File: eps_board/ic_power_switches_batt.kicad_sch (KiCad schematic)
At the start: 4 parts, among them U47 MCP23008T-E/SS

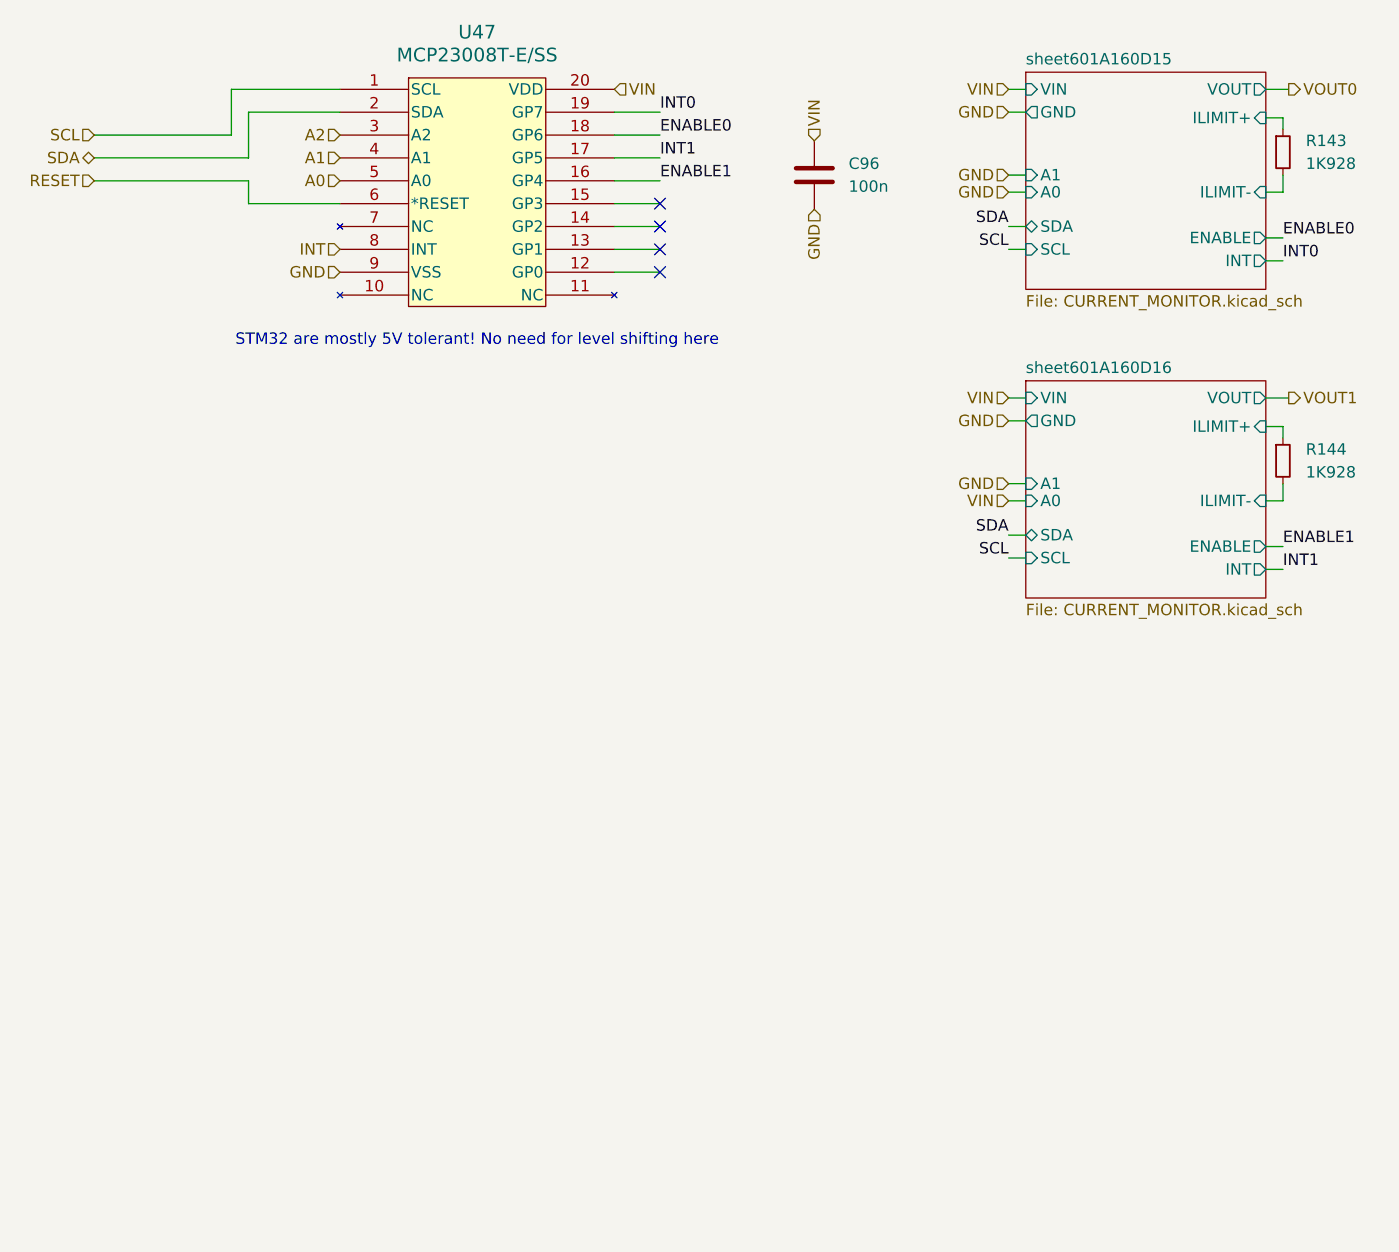
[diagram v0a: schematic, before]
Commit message: simply eps and automate startup conditions
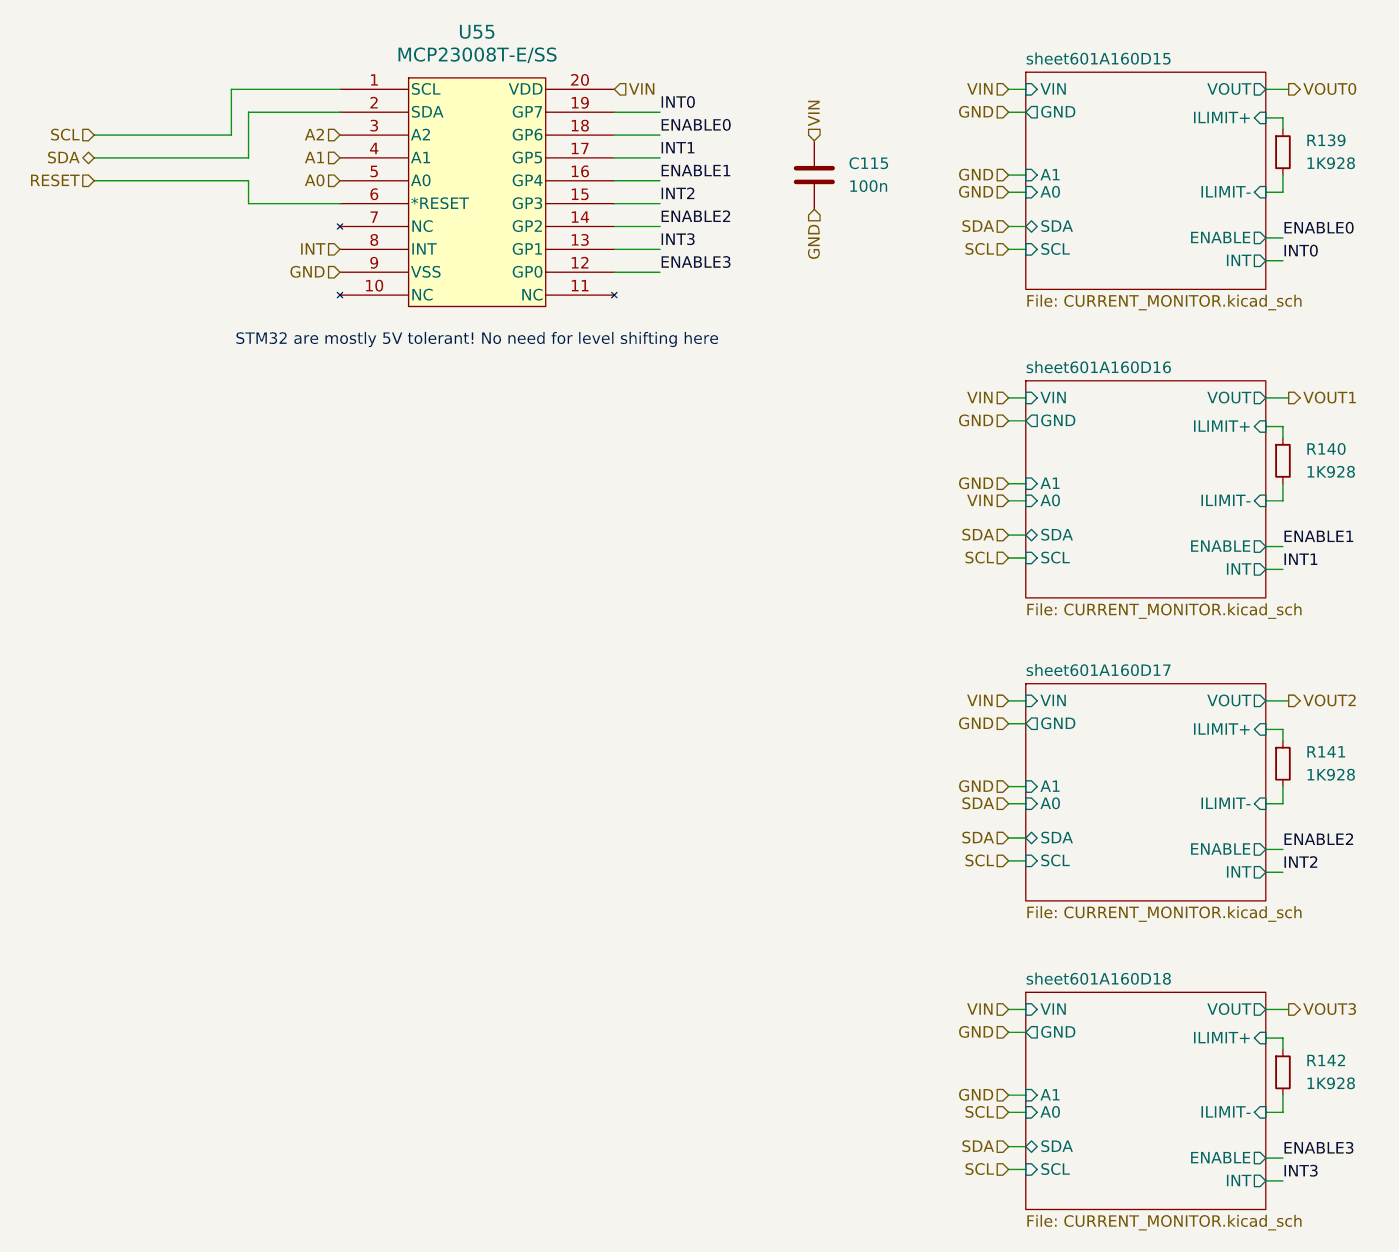
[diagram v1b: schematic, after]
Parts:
- added R141, R142: 1K928, Resistor_SMD:R_0603_1608Metric_Pad0.98x0.95mm_HandSolder, symbol Device:R_Small
- renumbered C96 to C115, R143 to R139, R144 to R140, U47 to U55
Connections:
- net ENABLE3: now reaches U55.12 (GP0)
- net INT3: now reaches U55.13 (GP1)
- net ENABLE2: now reaches U55.14 (GP2)
- net INT2: now reaches U55.15 (GP3)
- new net sheet601A160D17/ILIMIT+: R141.1
- new net sheet601A160D17/ILIMIT-: R141.2
- new net sheet601A160D18/ILIMIT+: R142.1
- new net sheet601A160D18/ILIMIT-: R142.2
- no-connect marks 4 -> 0
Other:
- added sheet sheet601A160D17 (CURRENT_MONITOR.kicad_sch)
- added sheet sheet601A160D18 (CURRENT_MONITOR.kicad_sch)

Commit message: pcb and silk screen cleanup, interim
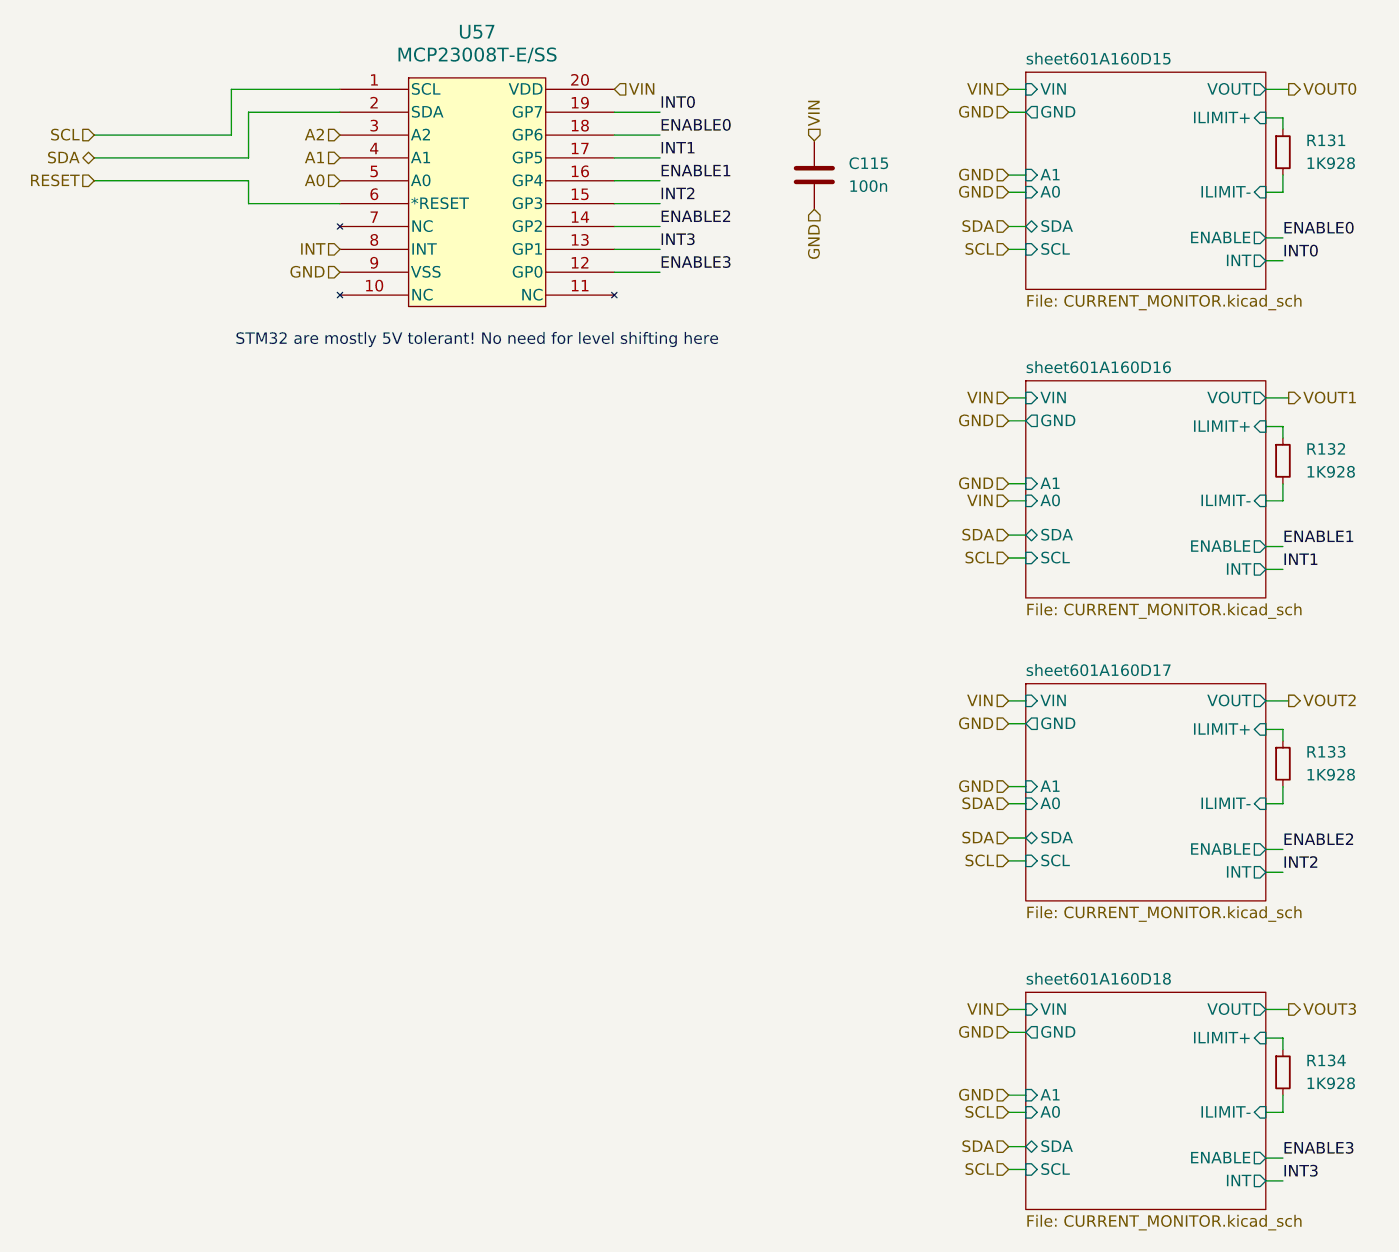
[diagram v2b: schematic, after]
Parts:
- renumbered R139 to R131, R140 to R132, R141 to R133, R142 to R134, U55 to U57
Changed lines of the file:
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@@
 		(dnp no)
 		(fields_autoplaced yes)
-		(property "Reference" "U55"
+		(property "Reference" "U57"
 			(at 84.455 26.67 0)
 			(effects
@@
 			(project "EPS"
 				(path "/05170af6-30ef-4c3a-b972-f098085da1bc/11ac4e4f-a41f-43ab-96d4-6191a21d3d63"
-					(reference "U55")
+					(reference "U57")
 					(unit 1)
 				)
@@
 		(dnp no)
 		(fields_autoplaced yes)
-		(property "Reference" "R139"
+		(property "Reference" "R131"
 			(at 176.53 38.7349 0)
 			(effects
@@
 			(project "EPS"
 				(path "/05170af6-30ef-4c3a-b972-f098085da1bc/11ac4e4f-a41f-43ab-96d4-6191a21d3d63"
-					(reference "R139")
+					(reference "R131")
 					(unit 1)
 				)
@@
 		(dnp no)
 		(fields_autoplaced yes)
-		(property "Reference" "R141"
+		(property "Reference" "R133"
 			(at 176.53 106.6799 0)
 			(effects
@@
 			(project "EPS"
 				(path "/05170af6-30ef-4c3a-b972-f098085da1bc/11ac4e4f-a41f-43ab-96d4-6191a21d3d63"
-					(reference "R141")
+					(reference "R133")
 					(unit 1)
 				)
@@
 		(dnp no)
 		(fields_autoplaced yes)
-		(property "Reference" "R142"
+		(property "Reference" "R134"
 			(at 176.53 140.9699 0)
 			(effects
@@
 			(project "EPS"
 				(path "/05170af6-30ef-4c3a-b972-f098085da1bc/11ac4e4f-a41f-43ab-96d4-6191a21d3d63"
-					(reference "R142")
+					(reference "R134")
 					(unit 1)
 				)
@@
 		(dnp no)
 		(fields_autoplaced yes)
-		(property "Reference" "R140"
+		(property "Reference" "R132"
 			(at 176.53 73.0249 0)
 			(effects
@@
 			(project "EPS"
 				(path "/05170af6-30ef-4c3a-b972-f098085da1bc/11ac4e4f-a41f-43ab-96d4-6191a21d3d63"
-					(reference "R140")
-					(unit 1)
-				)
+					(reference "R132")
+					(unit 1)
+				)

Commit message: light sensors with i2c multiplexers for AVI board. i2c amp/volt meter for attitude control coils
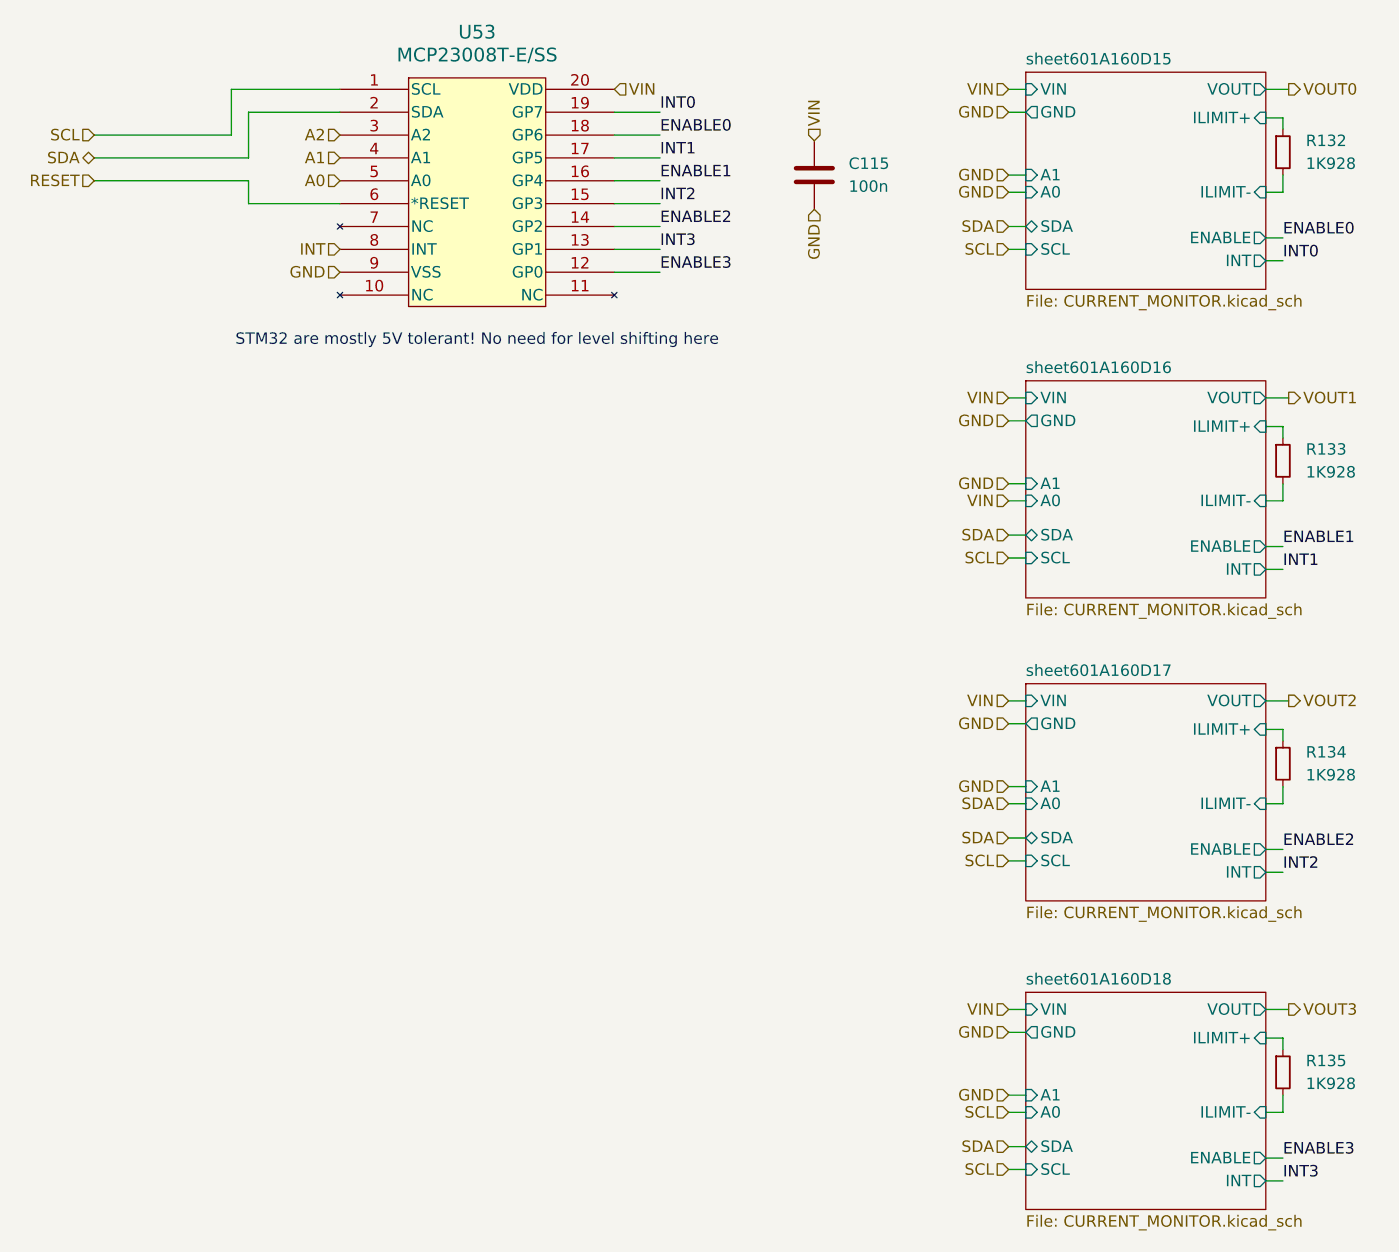
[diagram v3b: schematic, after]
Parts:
- renumbered R131 to R132, R132 to R133, R133 to R134, R134 to R135, U57 to U53
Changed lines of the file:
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@@
 		(dnp no)
 		(fields_autoplaced yes)
-		(property "Reference" "U57"
+		(property "Reference" "U53"
 			(at 84.455 26.67 0)
 			(effects
@@
 			(project "EPS"
 				(path "/05170af6-30ef-4c3a-b972-f098085da1bc/11ac4e4f-a41f-43ab-96d4-6191a21d3d63"
-					(reference "U57")
+					(reference "U53")
 					(unit 1)
 				)
@@
 		(dnp no)
 		(fields_autoplaced yes)
-		(property "Reference" "R131"
+		(property "Reference" "R132"
 			(at 176.53 38.7349 0)
 			(effects
@@
 			(project "EPS"
 				(path "/05170af6-30ef-4c3a-b972-f098085da1bc/11ac4e4f-a41f-43ab-96d4-6191a21d3d63"
-					(reference "R131")
+					(reference "R132")
 					(unit 1)
 				)
@@
 		(dnp no)
 		(fields_autoplaced yes)
-		(property "Reference" "R133"
+		(property "Reference" "R134"
 			(at 176.53 106.6799 0)
 			(effects
@@
 			(project "EPS"
 				(path "/05170af6-30ef-4c3a-b972-f098085da1bc/11ac4e4f-a41f-43ab-96d4-6191a21d3d63"
-					(reference "R133")
+					(reference "R134")
 					(unit 1)
 				)
@@
 		(dnp no)
 		(fields_autoplaced yes)
-		(property "Reference" "R134"
+		(property "Reference" "R135"
 			(at 176.53 140.9699 0)
 			(effects
@@
 			(project "EPS"
 				(path "/05170af6-30ef-4c3a-b972-f098085da1bc/11ac4e4f-a41f-43ab-96d4-6191a21d3d63"
-					(reference "R134")
+					(reference "R135")
 					(unit 1)
 				)
@@
 		(dnp no)
 		(fields_autoplaced yes)
-		(property "Reference" "R132"
+		(property "Reference" "R133"
 			(at 176.53 73.0249 0)
 			(effects
@@
 			(project "EPS"
 				(path "/05170af6-30ef-4c3a-b972-f098085da1bc/11ac4e4f-a41f-43ab-96d4-6191a21d3d63"
-					(reference "R132")
-					(unit 1)
-				)
+					(reference "R133")
+					(unit 1)
+				)
